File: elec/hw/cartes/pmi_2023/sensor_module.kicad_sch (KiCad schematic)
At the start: 30 parts, among them U12 LSM6DSO32XTR, U22 VL53L5CXV0GC, U30 VL53L5CXV0GC

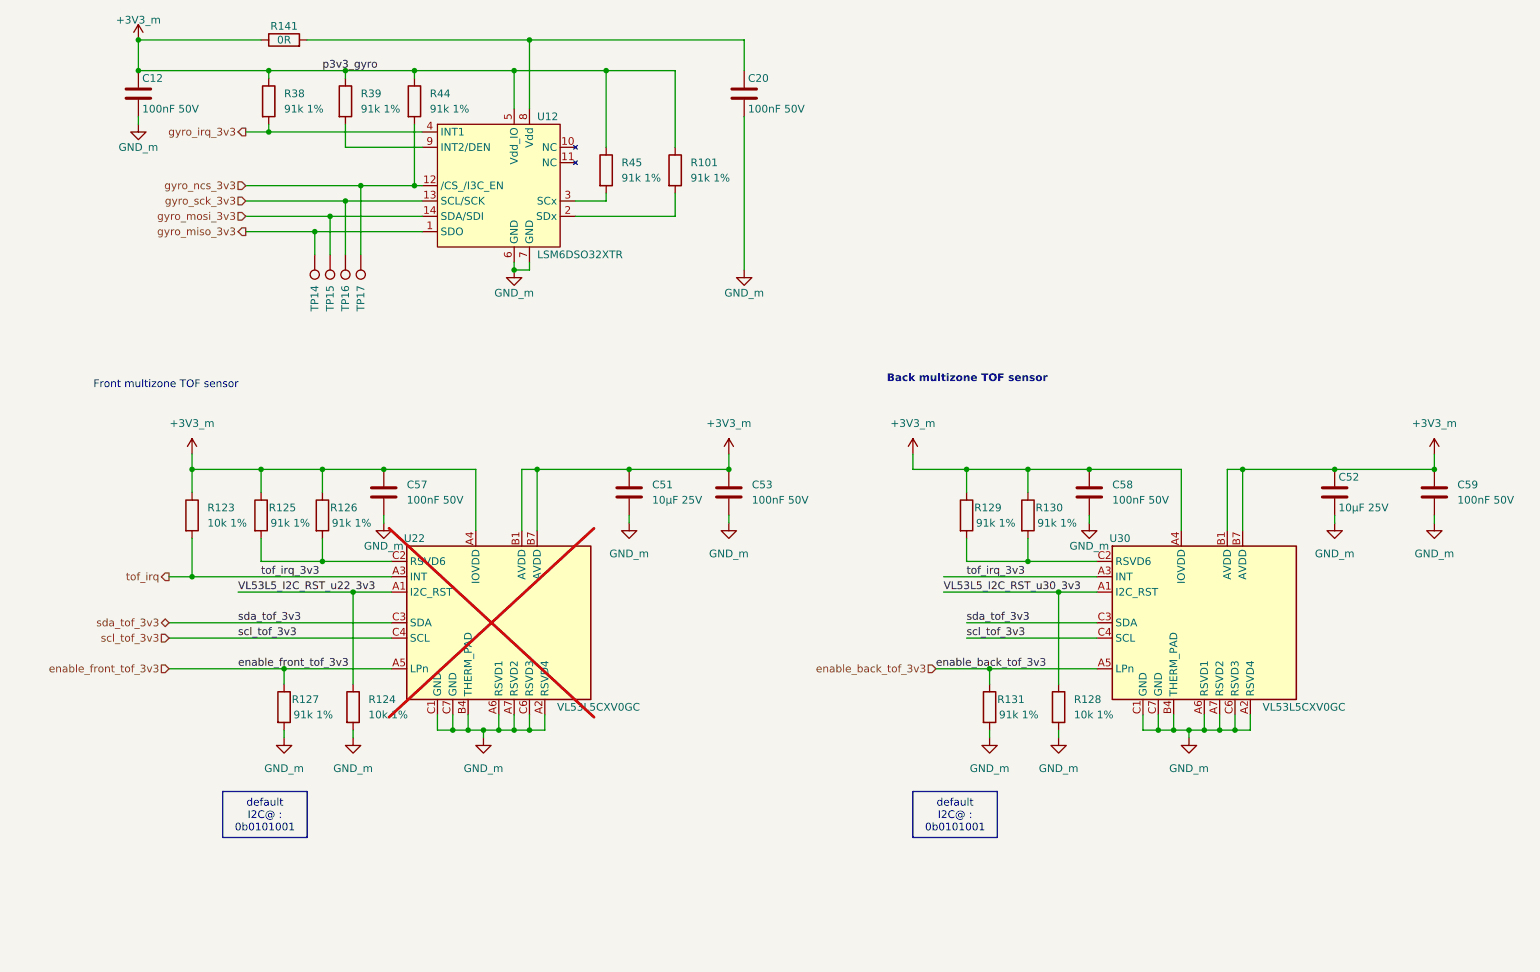
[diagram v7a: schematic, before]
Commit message: pmi : replaced accelerometer and gyroscope with BMI088
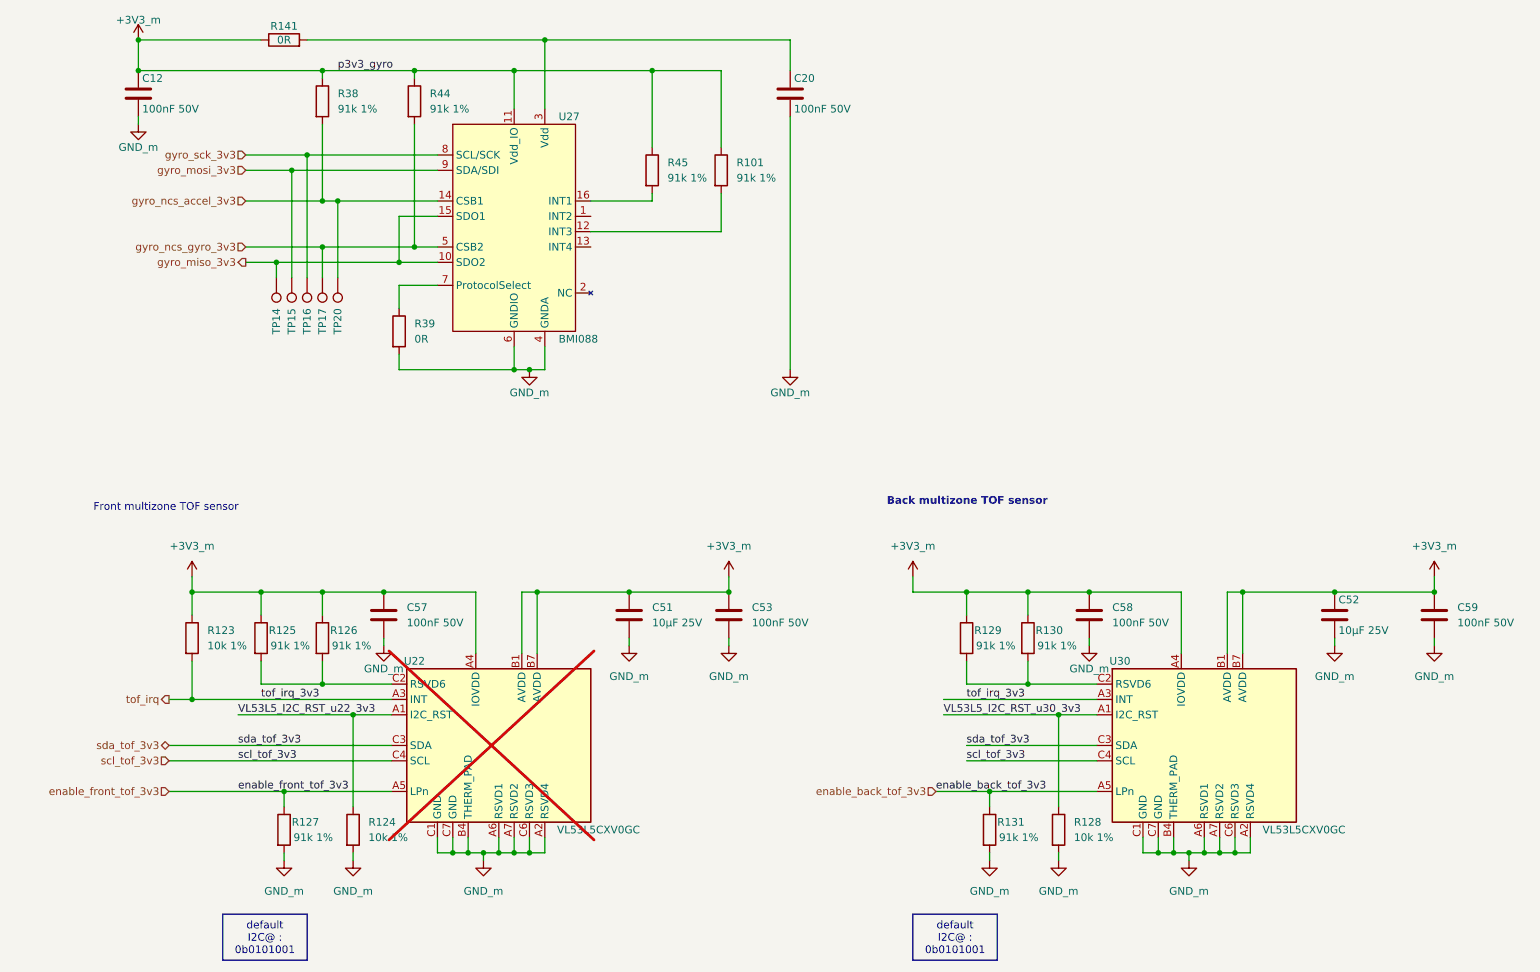
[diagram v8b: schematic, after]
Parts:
- removed R39: 91k 1%, cocotter_resistor:r0603_reflow, symbol cocotter_resistors:R_91k_0603_1%
- removed U12: LSM6DSO32XTR, cocotter_ic:LGA-14_3x2.5mm_P0.5mm_LayoutBorder3x4y, symbol cocotter_ic:LSM6DSO32XTR
- added R39: 0R, cocotter_resistor:r0603_reflow, symbol cocotter_resistors:R_0R_0603
- added TP20: TestPoint, cocotter_others:testpoint-THT-0.5mm, symbol cocotter_others:TestPoint
- added U27: BMI088, cocotter_ic:Bosch_LGA-16_4.5x3mm_P0.5mm_LayoutBorder7x1y_ClockwisePinNumbering, symbol cocotter_ic:BMI088
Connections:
- net +3V3_m: now also U27.11 (Vdd_IO)
- net GND_m: now also R39.2, U27.4 (GNDA), U27.6 (GNDIO)
- net gyro_miso_3v3: now also U27.10 (SDO2), U27.15 (SDO1)
- net gyro_mosi_3v3: now also U27.9 (SDA/SDI)
- net gyro_sck_3v3: now also U27.8 (SCL/SCK)
- net at C20.1, R141.2: now also U27.3 (Vdd)
- net at R45.2: now also U27.16 (INT1)
- net at R101.2: now also U27.12 (INT3)
- net gyro_irq_3v3 renamed gyro_ncs_accel_3v3
- net gyro_ncs_accel_3v3: now also TP20.1, U27.14 (CSB1)
- net gyro_ncs_3v3 renamed gyro_ncs_gyro_3v3
- net gyro_ncs_gyro_3v3: now also U27.5 (CSB2)
- new net: R39.1, U27.7 (ProtocolSelect)
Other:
- moved on the sheet: C20, C51, C52, C53, C57, C58, C59, R101, R123, R124, R125, R126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
